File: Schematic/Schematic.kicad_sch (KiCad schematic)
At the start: 12 parts, among them J1 Conn_01x04_Pin, U1 STM32F401CCUx

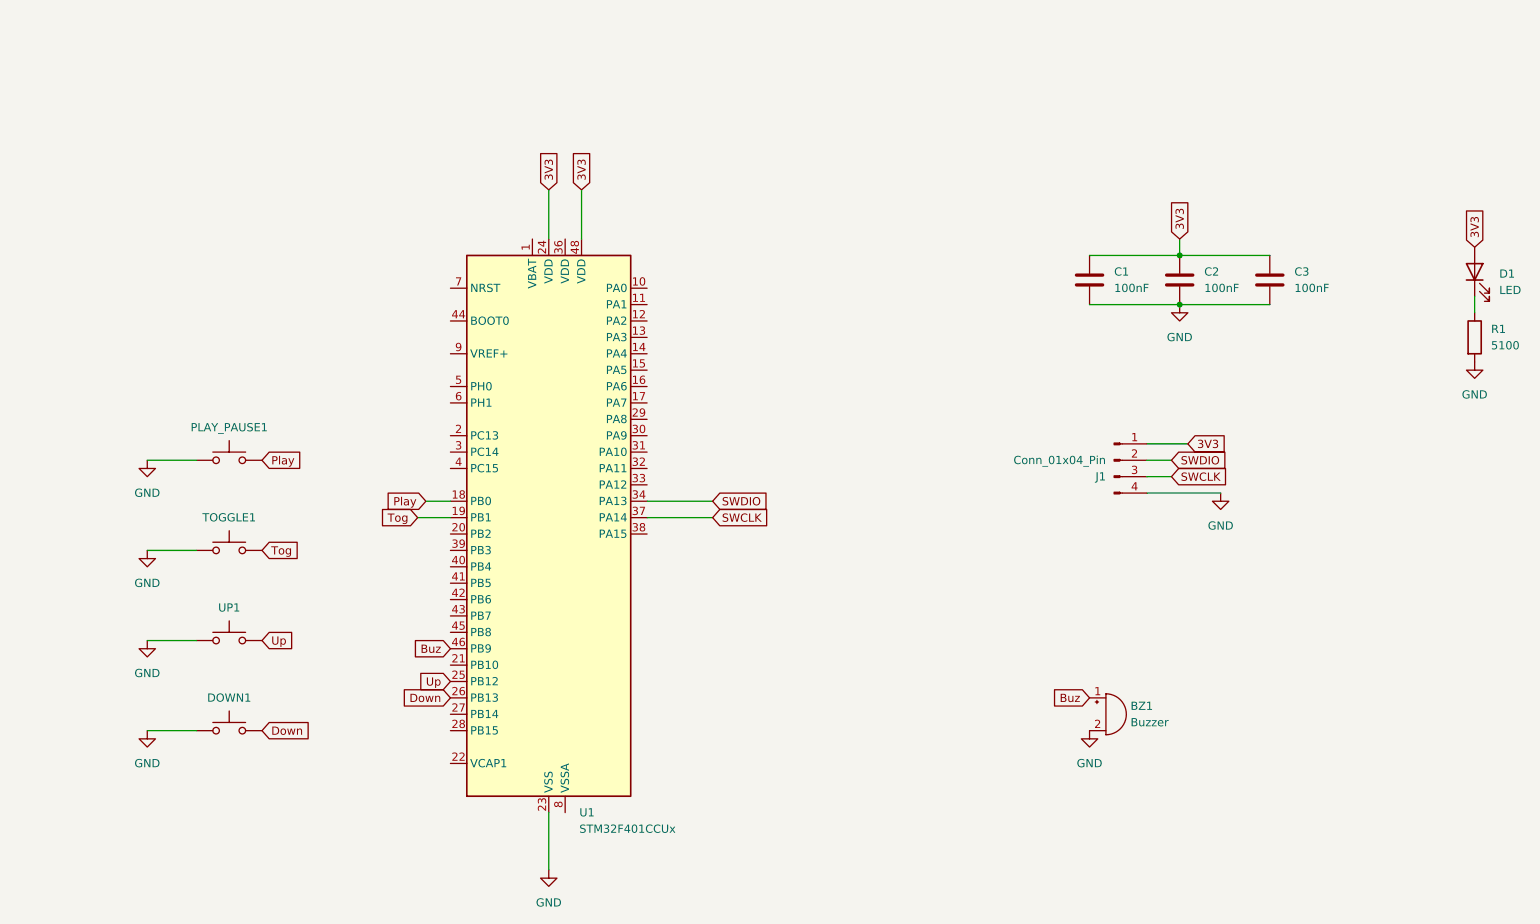
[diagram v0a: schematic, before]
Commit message: Debugging totalSprintTime_
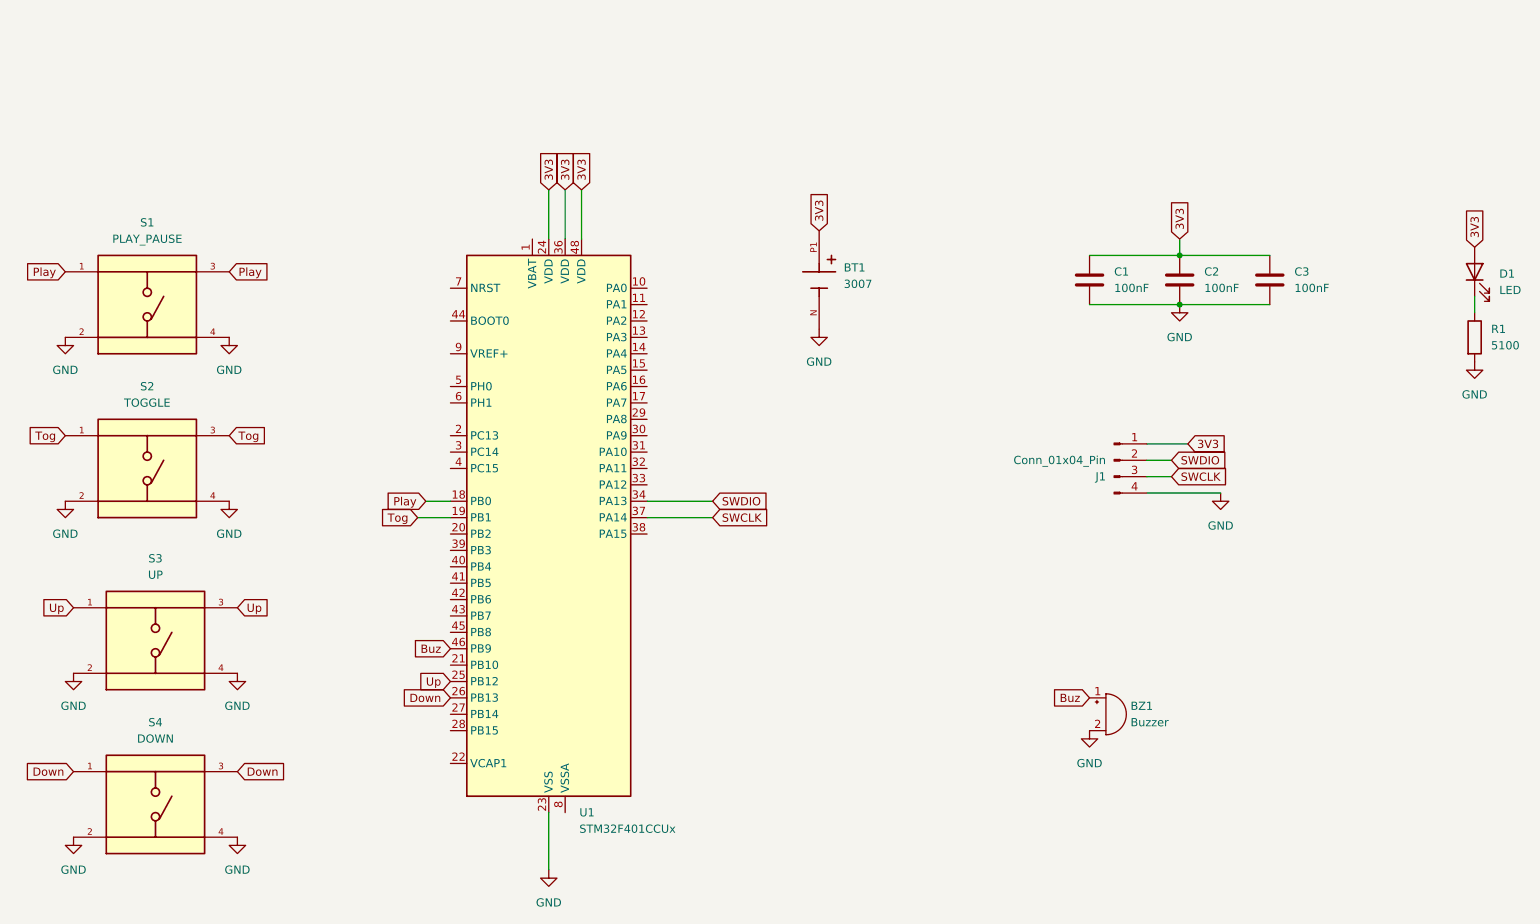
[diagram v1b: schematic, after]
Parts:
- removed DOWN1, PLAY_PAUSE1, TOGGLE1, UP1: SW_Push, Button_Switch_SMD:SW_Push_1TS009xxxx-xxxx-xxxx_6x6x5mm, symbol Switch:SW_Push
- added BT1: 3007, 3007:BAT_3007, symbol 3007:3007
- added S1: PLAY_PAUSE, TS04_66_73_BK_100_SMT:SW_TS04-66-73-BK-100-SMT, symbol TS04-66-73-BK-100-SMT:TS04-66-73-BK-100-SMT
- added S2: TOGGLE, TS04_66_73_BK_100_SMT:SW_TS04-66-73-BK-100-SMT, symbol TS04-66-73-BK-100-SMT:TS04-66-73-BK-100-SMT
- added S3: UP, TS04_66_73_BK_100_SMT:SW_TS04-66-73-BK-100-SMT, symbol TS04-66-73-BK-100-SMT:TS04-66-73-BK-100-SMT
- added S4: DOWN, TS04_66_73_BK_100_SMT:SW_TS04-66-73-BK-100-SMT, symbol TS04-66-73-BK-100-SMT:TS04-66-73-BK-100-SMT
- BZ1: footprint Buzzer_Beeper:Buzzer_D14mm_H7mm_P10mm -> Buzzer_Beeper:Buzzer_Mallory_AST1240MLQ
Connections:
- net 3V3: now also U1.36 (VDD), BT1.P1
- net Down: now also S4.1, S4.3
- net GND: now also BT1.N, S1.2, S1.4, S2.2, S2.4, S3.2, S3.4, S4.2, S4.4
- net Play: now also S1.1, S1.3
- net Tog: now also S2.1, S2.3
- net Up: now also S3.1, S3.3

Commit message: Schematic stuff
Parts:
- added C4, C5, C6: 100nF, Capacitor_SMD:C_0201_0603Metric, symbol Device:C
- added C7, C8: 4.7uF, Capacitor_SMD:C_0201_0603Metric, symbol Device:C
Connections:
- net 3V3: now also C4.1, C5.1, C6.1, C7.1
- net GND: now also C4.2, C5.2, C6.2, C7.2, C8.2
- net at U1.22 (VCAP1): now also C8.1
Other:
- moved on the sheet: C1, C2, C3
